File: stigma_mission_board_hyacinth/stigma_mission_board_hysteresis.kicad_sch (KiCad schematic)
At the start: 138 parts, among them J10 Conn_02x05_Top_Bottom_Mountin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, J13 SMA, J2 SMA, J3 Conn_02x04_Top_Bottom, J5 Conn_02x02_Top_Bottom, J6 JST-GH, J8 Conn_02x04_Top_Bottom, Q1 DMN2056U, U1 L7805, U12 LAN8742A, U13 TPD4E1U06, U14 INA181, U17 Ai-Thinker-Ra-01, U2 L7805, U3 Ai-Thinker-Ra-01, U4 SN74HCS594, U5 MCP2562-E-SN, U6 MCP2562-E-SN, U7 AZ1117H-ADJ, U8 AZ1117H-ADJ, Y1 25MHz

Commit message: fixed some errors
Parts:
- renumbered C31 to C1, C32 to C10, C34 to C11, C35 to C12, C54 to C13, C56 to C14, C58 to C15, C8 to C16, C2 to C17, C4 to C18, C47 to C19, C33 to C2, C12 to C20, C13 to C21, C14 to C22, C15 to C23, C37 to C24, C38 to C25, C39 to C26, C60 to C27, C61 to C28, C59 to C29, C46 to C3, C36 to C30, C5 to C31, C6 to C32, C64 to C33, C40 to C34, C41 to C35, C42 to C36, C43 to C37, C44 to C38, C45 to C39, C48 to C4, C9 to C40, C10 to C41, C11 to C42, C16 to C43, C55 to C5, C57 to C6, C1 to C7, C3 to C8, C7 to C9, D15 to D10, D5 to D11, D2 to D12, D21 to D13, D23 to D14, D20 to D15, D22 to D16, D19 to D2, D7 to D4, D8 to D5, D9 to D6, D10 to D7, D18 to D8, D4 to D9, J8 to J1, J13 to J10, J10 to J2, J1 to J4, J4 to J5, J9 to J6, J5 to J7, J2 to J8, J6 to J9, JP9 to JP1, JP10 to JP2, JP12 to JP3, JP11 to JP4, R60 to R10, R8 to R11, R27 to R12, R31 to R13, R57 to R14, R62 to R15, R58 to R16, R9 to R17, R3 to R18, R35 to R19, R4 to R2, R36 to R20, R55 to R21, R53 to R22, R48 to R23, R47 to R24, R46 to R25, R10 to R26, R41 to R27, R42 to R28, R43 to R29, R2 to R3, R44 to R30, R5 to R31, R45 to R32, R49 to R33, R50 to R34, R51 to R35, R52 to R36, R34 to R37, R54 to R38, R56 to R39, R59 to R4, R40 to R5, R37 to R6, R23 to R7, R30 to R8, R61 to R9, U6 to U10, U12 to U11, U17 to U12, U4 to U2, U2 to U3, U7 to U4, U14 to U5, U8 to U6, U5 to U7, U3 to U8, U13 to U9
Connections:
- net GND: now also J2.MP (MountPin)
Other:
- note added: "unused"
- note removed: "@todo should we rather measure current than voltage?"
- moved on the sheet: C11, C13, C2, C4

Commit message: add rj45 connector
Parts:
- removed J9: JST-GH, Connector_JST:JST_GH_SM04B-GHS-TB_1x04-1MP_P1.25mm_Horizontal, symbol Connector_Generic_MountingPin:Conn_01x04_MountingPin
- added R60, R62: 270, Resistor_SMD:R_0603_1608Metric, symbol Device:R
- added R61: 10k, Resistor_SMD:R_0603_1608Metric, symbol Device:R
- added RJ45: ~, ProLib_pcs_2025-02-16:RJ45-TH_MJ88B-B011-RVL11-P, symbol my_symbols:MJ88B-B011-RVL11-P
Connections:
- net GND: now also R60.2, R61.2, R62.2, RJ45.13 (SHELL), RJ45.14 (SHELL), RJ45.8
- net RXN: now also RJ45.6
- net RXP: now also RJ45.3
- net TXN: now also RJ45.2
- net TXP: now also RJ45.1
- net at C24.1, C25.1, C26.1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: now also RJ45.4, RJ45.5
- net ETH_LED_1: no longer names the net of U11.3 (LED1/REGOFF)
- net ETH_LED_1: now also RJ45.9 (L+)
- net ETH_LED_2 renamed ETH_nINT
- net ETH_nINT: now also R61.1, RJ45.12 (R-)
- new net: R60.1, RJ45.10 (L-)
- new net: R62.1, RJ45.11 (R+)
- no-connect marks 12 -> 13
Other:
- note added: "@TODO: - verify that RJ45 pinout is correct"
- note removed: "@TODO: - connector - LEDs"
- note removed: "@todo connector wählen"
- moved on the sheet: C36, C37, R19, R20, Y1

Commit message: placed recovery outputs and vehicle bus, fixed errors in schematic
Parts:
- removed D10, D14: SVT12100, Package_TO_SOT_SMD:TO-277B, symbol Device:D
- added D10, D14: SS34, Diode_SMD:D_SMA, symbol Diode:SS34
- JP3, JP4: value SolderJumper_3_Bridged12 -> servo_switch; footprint Jumper:SolderJumper-3_P1.3mm_Bridged12_Pad1.0x1.5mm -> Jumper:SolderJumper-3_P1.3mm_Open_RoundedPad1.0x1.5mm; LCSC# (none) -> x; now in the parts list
- RJ45: footprint ProLib_pcs_2025-02-16:RJ45-TH_MJ88B-B011-RVL11-P -> Stigma:RJ45-TH_MJ88B-B011-RVL11-P
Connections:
- net +3V3 is gone; now on net +3.3V: C38.2, C39.2, C42.2, C43.2, U12.3 (VDD), U8.3 (VDD)
- net v_main_pre_sense: now also D10.1 (K), D14.1 (K)
- net at JP2.1 (A): now also D14.2 (A)
- net at JP1.1 (A): now also D10.2 (A)
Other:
- note added: "differential pair!"
- note added: "length relevant"

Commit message: made board more compact, started routing recovery outputs
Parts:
- removed J7: Conn_02x02_Top_Bottom, Connector_Molex:Molex_Micro-Fit_3.0_43045-0400_2x02_P3.00mm_Horizontal, symbol Connector_Generic:Conn_02x02_Top_Bottom
- removed JP3, JP4: servo_switch, Jumper:SolderJumper-3_P1.3mm_Open_RoundedPad1.0x1.5mm, symbol Jumper:SolderJumper_3_Bridged12
- added F1, F2, F3, F4, F5, F6, F7, F8: 10A, Fuse:Fuse_1206_3216Metric, symbol Device:Fuse_Small
- added J7: JST-GH 4Pin, Connector_JST:JST_GH_BM04B-GHS-TBT_1x04-1MP_P1.25mm_Vertical, symbol Connector:Conn_01x04_Pin
- J2: footprint Connector_Molex:Molex_Micro-Fit_3.0_43045-1010_2x05-1MP_P3.00mm_Horizontal -> stigma:DF40GB-10DP-0.4V-plug
- RJ1: renamed from RJ45; footprint Stigma:RJ45-TH_MJ88B-B011-RVL11-P -> stigma:RJ45-TH_MJ88B-B011-RVL11-P
- renumbered C36 to C31, C37 to C32, C31 to C33, C32 to C34, C33 to C35, C34 to C36, C35 to C37, J10 to J9, R19 to R17, R20 to R18, R17 to R19, R18 to R20, R61 to R39, R60 to R40, R62 to R41, R39 to R42
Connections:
- net +5V: now also F2.2, F6.2, J7.1 (Pin_1)
- net DAC: now also J7.2 (Pin_2)
- net GND: now also J2.s (shield), J7.3 (Pin_3), J7.4 (Pin_4); no longer J2.MP (MountPin)
- net Recovery Output 4/high_current: now also F7.1, F8.2
- net Recovery Output2/high_current: now also F3.1, F4.2
- net high_current: now also F1.2, F3.2, F5.2, F7.2
- net high_current_2: now also F4.1, F8.1
- new net: BZ1.3, BZ1.4
- new net Recovery Output 1/high_current: F1.1, F2.1
- new net Recovery Output3/high_current: F5.1, F6.1

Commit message: some tydiing up and adding footprints
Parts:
- added R4: 100k, Resistor_SMD:R_0603_1608Metric, symbol Device:R_Small
- added R5: 10k, Resistor_SMD:R_0603_1608Metric, symbol Device:R_Small
- F2, F4, F6, F8: now not fitted
- renumbered R8 to R10, R9 to R11, R10 to R12, R11 to R13, R12 to R14, R13 to R15, R14 to R16, R15 to R17, R16 to R18, R17 to R19, R18 to R20, R19 to R21, R20 to R22, R21 to R23, R22 to R24, R23 to R25, R24 to R26, R25 to R27, R26 to R28, R27 to R29, R28 to R30, R29 to R31, R30 to R32, R31 to R33, R32 to R34, R33 to R35, R34 to R36, R35 to R37, R36 to R38, R37 to R39, R38 to R40, R39 to R41, R40 to R42, R41 to R43, R42 to R44, R4 to R6, R5 to R7, R6 to R8, R7 to R9
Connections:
- net GND: now also R5.2
- net high_current: now also R4.1
- net @TODO Free-ADC renamed ADC_HIGH_CURRENT2
- net ADC_HIGH_CURRENT2: now also R4.2, R5.1

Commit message: added the other 2 recovery outputs and sorted all components
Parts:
- J2: footprint stigma:DF40GB-10DP-0.4V-plug -> Stigma:DF40GB-10DP-0.4V-plug
- RJ1: footprint stigma:RJ45-TH_MJ88B-B011-RVL11-P -> Stigma:RJ45-TH_MJ88B-B011-RVL11-P
- renumbered C24 to C1, C30 to C10, C19 to C11, C31 to C12, C32 to C13, C20 to C14, C22 to C15, C7 to C16, C8 to C18, C18 to C19, C25 to C2, C21 to C20, C23 to C21, C33 to C22, C40 to C23, C34 to C24, C41 to C25, C38 to C26, C42 to C27, C39 to C28, C43 to C29, C35 to C3, C1 to C30, C10 to C31, C2 to C32, C11 to C33, C12 to C34, C3 to C35, C13 to C36, C4 to C37, C5 to C38, C14 to C39, C26 to C4, C6 to C40, C15 to C41, C16 to C42, C9 to C43, C36 to C5, C27 to C6, C37 to C7, C28 to C8, C29 to C9, D4 to D1, D15 to D10, D13 to D11, D16 to D12, D10 to D13, D2 to D14, D14 to D15, D11 to D16, D5 to D2, D6 to D3, D7 to D4, D1 to D5, D8 to D6, D3 to D7, D9 to D8, D12 to D9, F5 to F2, F2 to F3, F6 to F4, F3 to F5, F4 to F6, J4 to J1, J5 to J3, J6 to J4, J1 to J5, J3 to J6, J8 to J7, J9 to J8, J7 to J9, R34 to R1, R26 to R10, R27 to R11, R8 to R12, R29 to R13, R30 to R14, R39 to R15, R31 to R16, R32 to R17, R44 to R18, R9 to R19, R35 to R2, R14 to R20, R19 to R21, R41 to R22, R4 to R23, R5 to R24, R10 to R25, R15 to R26, R20 to R27, R42 to R28, R43 to R29, R36 to R3, R6 to R30, R12 to R31, R16 to R32, R18 to R33, R1 to R34, R3 to R35, R11 to R36, R17 to R37, R22 to R38, R33 to R39, R37 to R4, R21 to R40, R28 to R41, R2 to R42, R13 to R43, R7 to R44, R38 to R5, R23 to R6, R40 to R7, R24 to R8, R25 to R9, U11 to U1, U7 to U10, U10 to U11, U2 to U12, U5 to U2, U9 to U3, U1 to U4, U3 to U5, U4 to U6, U6 to U7, U12 to U9

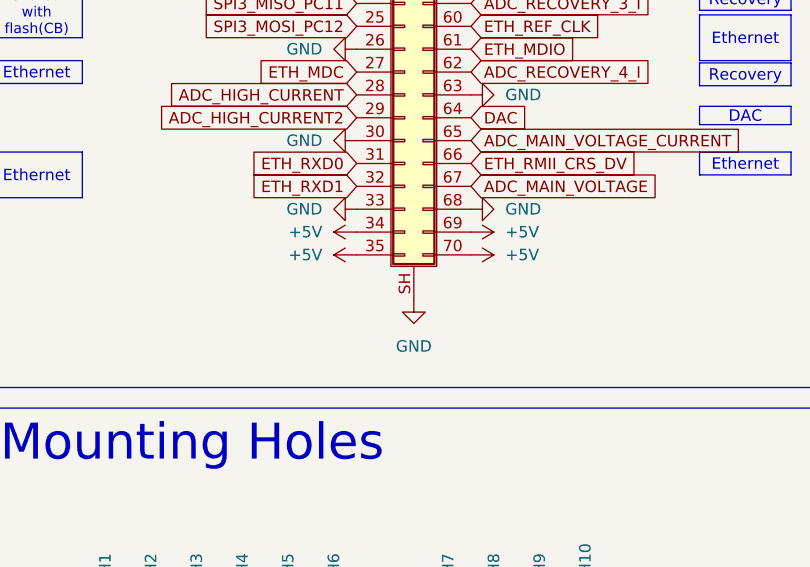
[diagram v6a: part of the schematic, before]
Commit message: added gps footprint
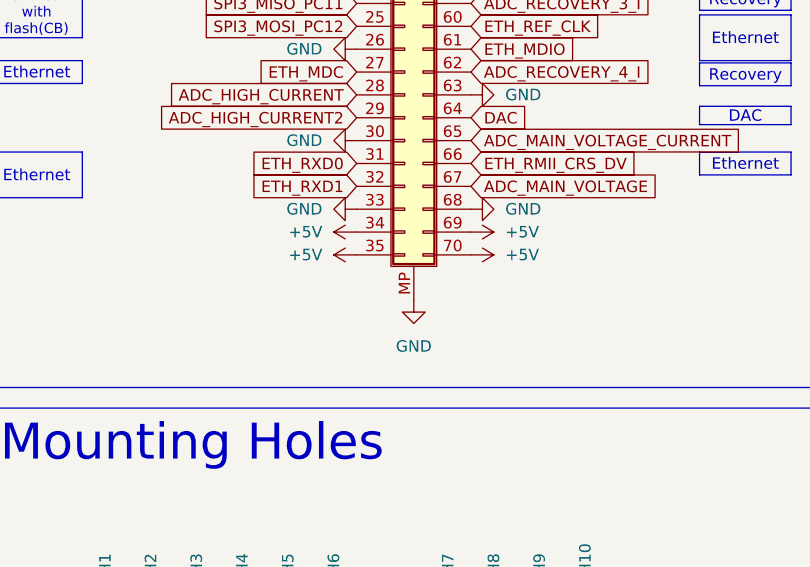
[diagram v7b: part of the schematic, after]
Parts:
- J1: footprint Stigma:DF40GB-70DP-0.4V-plug -> stigma:core-board
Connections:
- net GND: now also J1.MP (Shield); no longer J1.SH (Shield)
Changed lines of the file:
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@@
 			)
 		)
-		(property "Footprint" "Stigma:DF40GB-70DP-0.4V-plug"
+		(property "Footprint" "stigma:core-board"
 			(at 66.04 74.93 0)
 			(effects
@@
 		(pin "63"
 		)
-		(pin "SH"
+		(pin "MP"
 		)
 		(instances

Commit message: added GPS and Coreboard connector, changed ROs
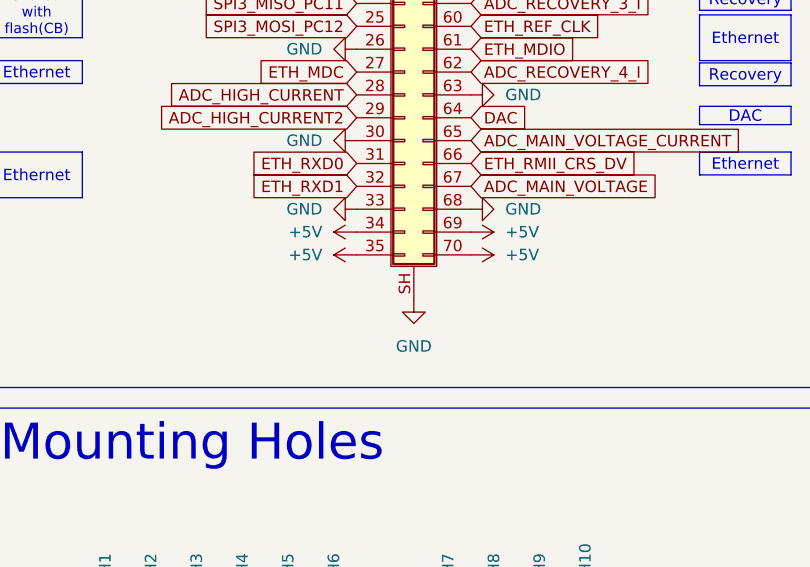
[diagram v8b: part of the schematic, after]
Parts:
- J1: footprint stigma:core-board -> Stigma:core-board
- J2: footprint Stigma:DF40GB-10DP-0.4V-plug -> Stigma:gps-board-outer-mounting-holes
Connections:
- net GND: now also J1.SH (Shield); no longer J1.MP (Shield)
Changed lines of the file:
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@@
 			)
 		)
-		(property "Footprint" "Stigma:DF40GB-10DP-0.4V-plug"
+		(property "Footprint" "Stigma:gps-board-outer-mounting-holes"
 			(at 162.56 43.18 0)
 			(effects
@@
 			)
 		)
-		(property "Footprint" "stigma:core-board"
+		(property "Footprint" "Stigma:core-board"
 			(at 66.04 74.93 0)
 			(effects
@@
 		(pin "63"
 		)
-		(pin "MP"
+		(pin "SH"
 		)
 		(instances
